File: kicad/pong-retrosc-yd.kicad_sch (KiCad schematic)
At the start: 24 parts, among them J1 RCA video (na placa), J4 chave A/B (painel), J5 pot P1 (painel), J6 pot P2 (painel), J7 START (painel), J8 RCA audio L (na placa), J9 RCA audio R (na placa), SW1 START, SW2 A/B, U1 RaspberryPi_Pico, U2 PAM8403 HW-012

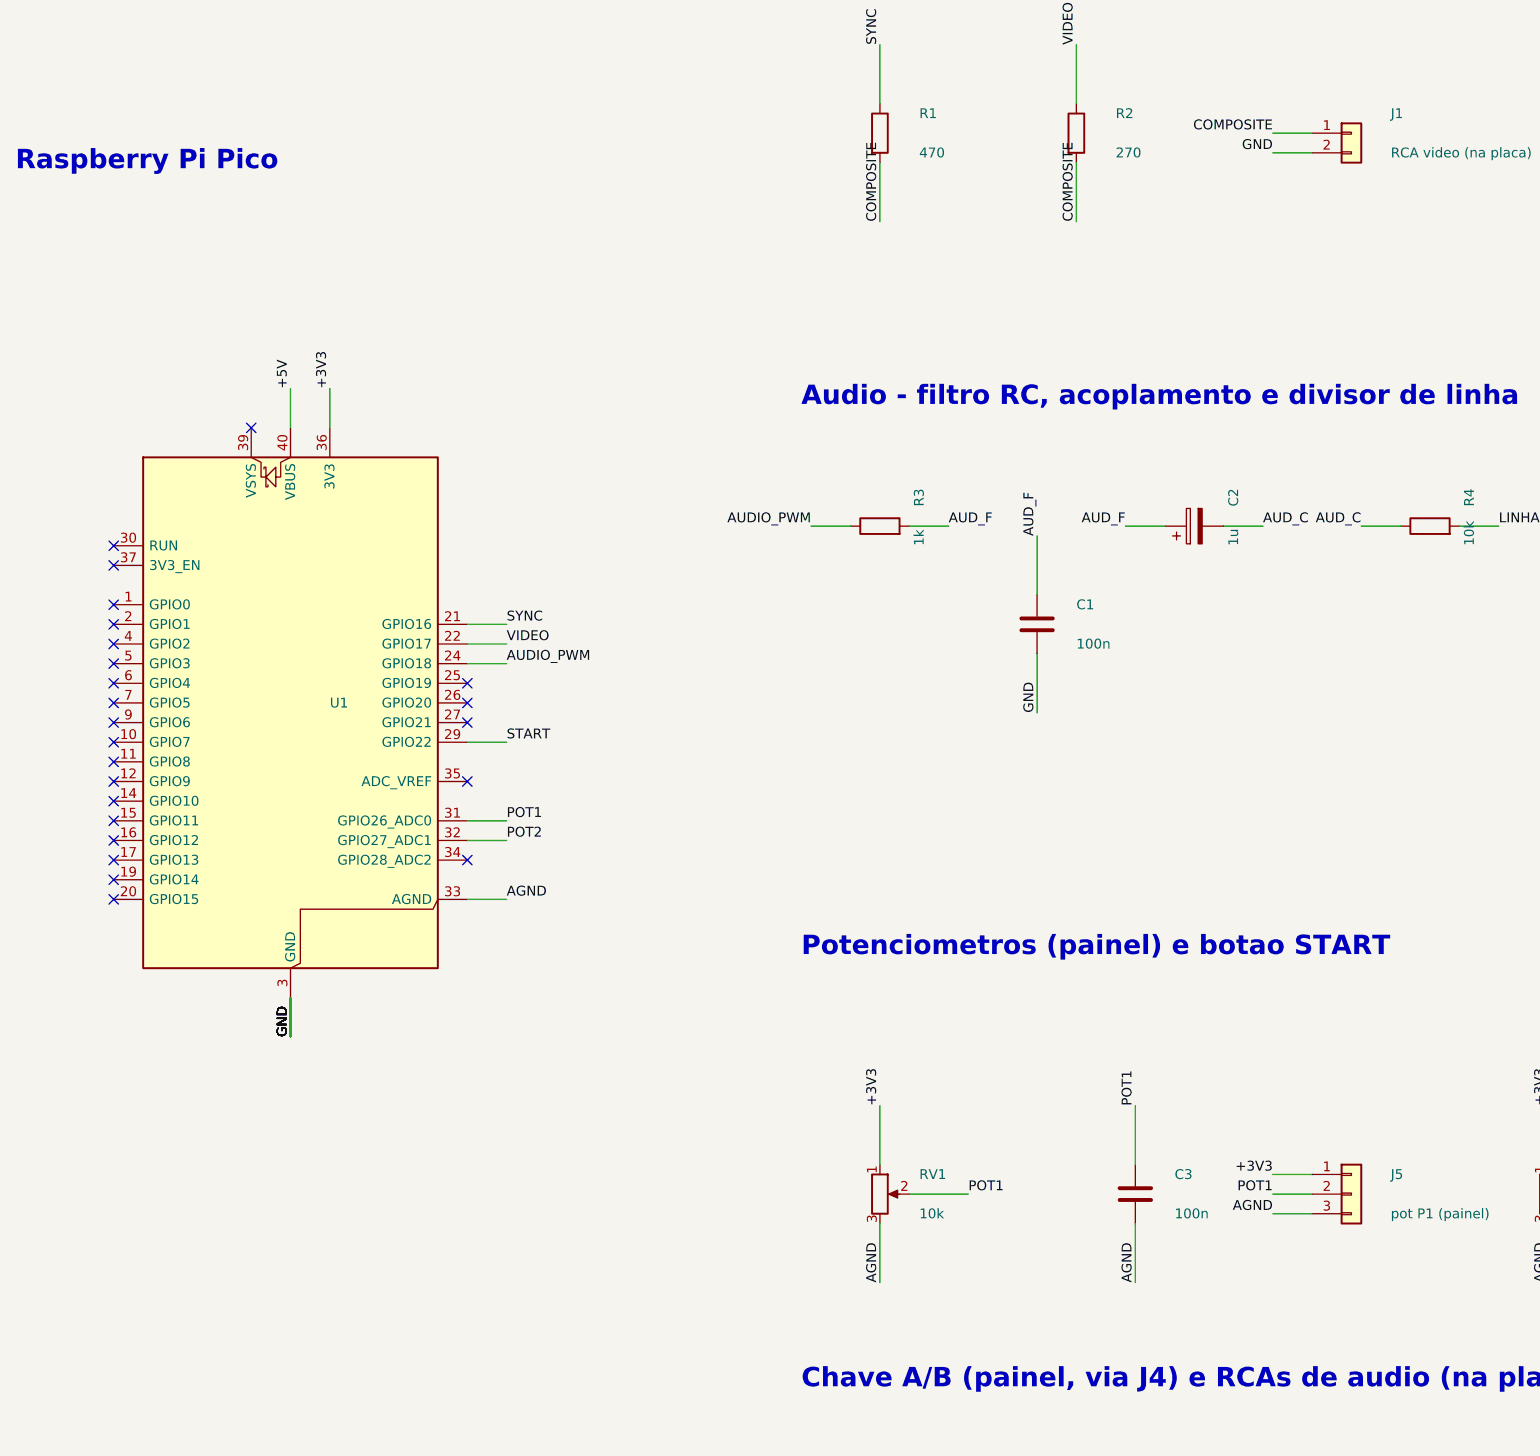
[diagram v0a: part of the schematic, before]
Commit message: kicad: variante para o RP2040 roxo + pinagem dos 3 modulos
Os clones do Pico tem a MESMA furacao mas outra funcao em cada posicao
de pino, entao o pipeline passa a gerar duas placas (--yd nos scripts):

- oficial (pong-retrosc): Raspberry Pi Pico e tambem a YD-RP2040 de 3
  botoes, cuja pinagem coincide em todas as posicoes que o projeto usa
- roxa 1 botao (pong-retrosc-yd): SYNC/VIDEO/AUDIO em 19/20/21, START em
  25, pots em 30/31, AGND em 29 e GND so em 6/15/35/38

Detalhes:
- a variante usa simbolo de conector 2x20 no lugar do simbolo do Pico:
  este une os pinos de mesmo nome (os 8 GND), o que amarraria GPIOs da
  roxa ao plano de terra
- marcas GP17/GP18 no silk das duas placas para conferir, antes de
  soldar, se placa e modulo sao da mesma variante
- docs/pinout.md com a pinagem completa dos 3 modulos lado a lado e as
  ressalvas da YD de 3 botoes (GP23=WS2812, pino 40 = Vout)
- tools/dsn_tweak.py versionado: a roxa precisa de trilha 0,25 mm no
  roteamento (com 0,30 o net START nao fecha)

DRC 0 erros e 0 desconectados nas duas placas; gerbers + zip de cada uma.

Co-Authored-By: Claude Opus 4.8 <noreply@anthropic.com>
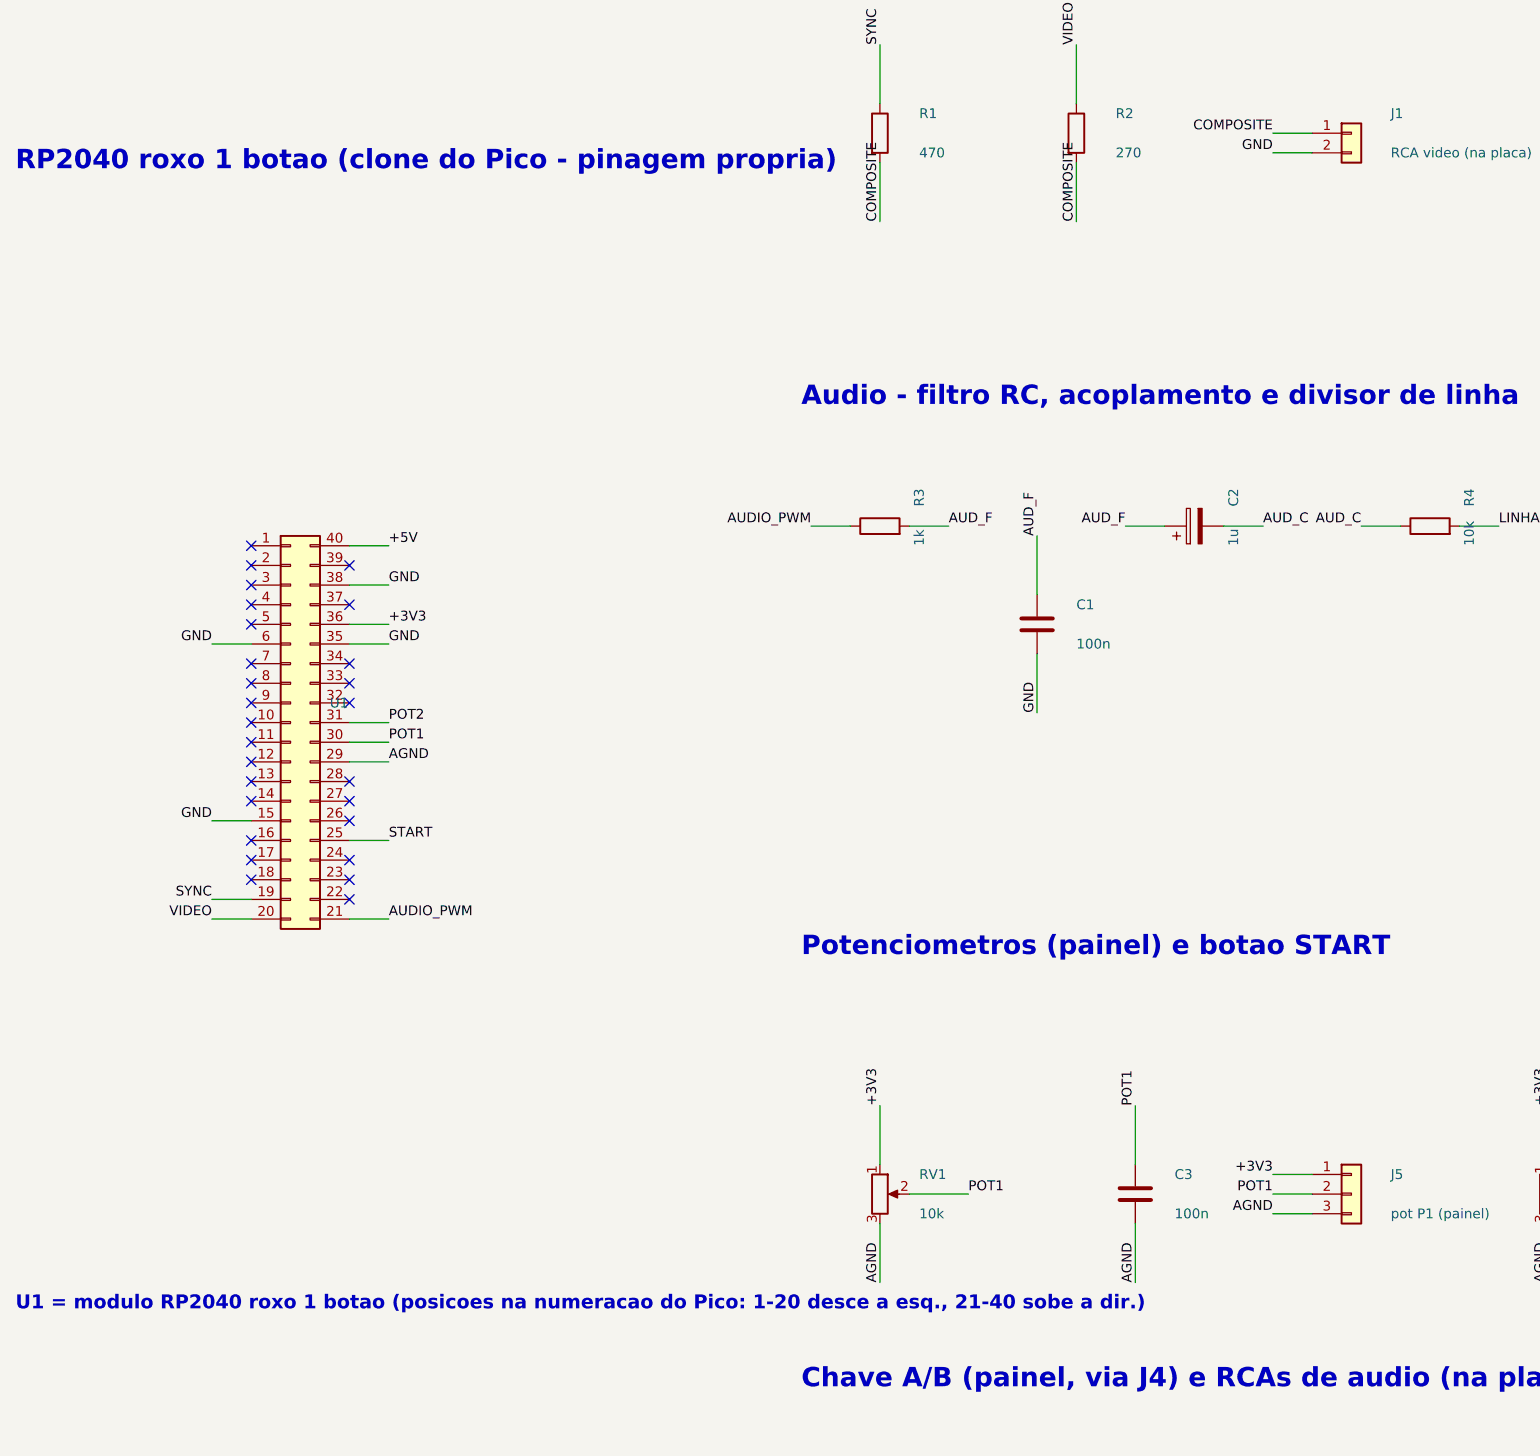
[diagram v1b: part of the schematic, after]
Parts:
- removed U1: RaspberryPi_Pico, Module:RaspberryPi_Pico_Common_THT, symbol MCU_Module:RaspberryPi_Pico
- added U1: RP2040 roxo 1 botao, Module:RaspberryPi_Pico_Common_THT, symbol Connector_Generic:Conn_02x20_Counter_Clockwise
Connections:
- net +3V3: now also U1.36 (Pin_36)
- net +5V: now also U1.40 (Pin_40)
- net AGND: now also U1.29 (Pin_29)
- net AUDIO_PWM: now also U1.21 (Pin_21)
- net GND: now also U1.15 (Pin_15), U1.35 (Pin_35), U1.38 (Pin_38), U1.6 (Pin_6)
- net POT1: now also U1.30 (Pin_30)
- net POT2: now also U1.31 (Pin_31)
- net START: now also U1.25 (Pin_25)
- net SYNC: now also U1.19 (Pin_19)
- net VIDEO: now also U1.20 (Pin_20)
- no-connect marks 26 -> 29
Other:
- note added: "RP2040 roxo 1 botao (clone do Pico - pinagem propria)"
- note added: "U1 = modulo RP2040 roxo 1 botao (posicoes na numeracao do Pico: 1-20 desce a esq., 21-40 sobe a dir.)"
- note removed: "Raspberry Pi Pico"
- title: RetroSC Pong - RP2040 -> RetroSC Pong - RP2040 (RP2040 roxo 1 botao)
